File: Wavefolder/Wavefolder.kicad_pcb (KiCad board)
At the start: 2 copper layers, 25 x 200 mm, 39 parts, among them J1 Sig1, J2 EuroPower, J3 Sig2, J4 Out1, J5 Out2, J6 CV2, Q1 BC547, Q2 BC557, Q3 BC557, Q4 BC547, Q5 BC557, Q6 BC547, U1 TL074, U2 TL082, U3 TL074

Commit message: Wavefolder layout
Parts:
- removed D6: LED, LED_SMD:LED_1206_3216Metric_ReverseMount_Hole1.8x2.4mm
- removed R10: 1k, Resistor_SMD:R_1206_3216Metric_Pad1.42x1.75mm_HandSolder
- added D1: 1N4148, Diode_THT:D_DO-35_SOD27_P7.62mm_Horizontal, F.Cu at (21.1, 120.6)
- added D2: 1N4148, Diode_THT:D_DO-35_SOD27_P7.62mm_Horizontal, F.Cu at (35.7, 105.3)
- added D4: 1N4148, Diode_THT:D_DO-35_SOD27_P7.62mm_Horizontal, F.Cu at (33.2, 105.3)
- added R15: 100k, Resistor_SMD:R_1206_3216Metric_Pad1.42x1.75mm_HandSolder, B.Cu at (13.4, 180.3)
- added R16: 100k, Resistor_SMD:R_1206_3216Metric_Pad1.42x1.75mm_HandSolder, B.Cu at (14.1, 175.3)
- added R17: 100k, Resistor_THT:R_Axial_DIN0204_L3.6mm_D1.6mm_P7.62mm_Horizontal, F.Cu at (26.1, 115.6)
- added R18: 100k, Resistor_THT:R_Axial_DIN0204_L3.6mm_D1.6mm_P7.62mm_Horizontal, F.Cu at (24.0, 115.6)
- added R19: 100k, Resistor_THT:R_Axial_DIN0204_L3.6mm_D1.6mm_P7.62mm_Horizontal, F.Cu at (26.5, 102.8)
- added R20: 100k, Resistor_THT:R_Axial_DIN0204_L3.6mm_D1.6mm_P7.62mm_Horizontal, F.Cu at (28.4, 102.8)
- added R21: 100k, Resistor_THT:R_Axial_DIN0204_L3.6mm_D1.6mm_P2.54mm_Vertical, F.Cu at (16.8, 102.8)
- added R22: 100k, Resistor_THT:R_Axial_DIN0204_L3.6mm_D1.6mm_P7.62mm_Horizontal, B.Cu at (22.8, 110.4)
- added R23: 15k, Resistor_THT:R_Axial_DIN0204_L3.6mm_D1.6mm_P7.62mm_Horizontal, B.Cu at (22.8, 108.0)
- added R24: 15k, Resistor_THT:R_Axial_DIN0204_L3.6mm_D1.6mm_P7.62mm_Horizontal, B.Cu at (32.8, 110.3)
- added R25: 1k, Resistor_SMD:R_1206_3216Metric_Pad1.42x1.75mm_HandSolder, B.Cu at (14.2, 201.5)
- added R26: 100k, Resistor_SMD:R_1206_3216Metric_Pad1.42x1.75mm_HandSolder, B.Cu at (13.8, 163.7)
- added R27: 100k, Resistor_SMD:R_1206_3216Metric_Pad1.42x1.75mm_HandSolder, B.Cu at (28.8, 145.1)
- added R28: 100k, Resistor_SMD:R_1206_3216Metric_Pad1.42x1.75mm_HandSolder, B.Cu at (28.2, 140.1)
- added R29: 100k, Resistor_SMD:R_1206_3216Metric_Pad1.42x1.75mm_HandSolder, B.Cu at (28.9, 135.0)
- added U4: TL082, Package_SO:SOIC-8_3.9x4.9mm_P1.27mm, B.Cu at (14.9, 187.0)
- R1, R11, R12, R13, R14, R2, R5, R6, R8, R9: footprint Resistor_THT:R_Axial_DIN0204_L3.6mm_D1.6mm_P7.62mm_Horizontal -> Resistor_THT:R_Axial_DIN0204_L3.6mm_D1.6mm_P2.54mm_Vertical
- R3: moved to B.Cu
- R4, R7: footprint Resistor_THT:R_Axial_DIN0204_L3.6mm_D1.6mm_P7.62mm_Horizontal -> Resistor_THT:R_Axial_DIN0204_L3.6mm_D1.6mm_P2.54mm_Vertical; moved to B.Cu
- U2: footprint Package_DIP:DIP-8_W7.62mm_LongPads -> Package_SO:SOIC-8_3.9x4.9mm_P1.27mm; moved to B.Cu
- moved C1 60.8 mm to (2.40, 87.6)
- moved C2 60.8 mm to (7.80, 88.1)
- moved R1 39.0 mm to (19.7, 92.9), turned to 270 degrees
- moved R14 37.5 mm to (16.4, 79.6), turned to 0 degrees
- moved D3 33.9 mm to (13.7, 118.0)
- moved R11 33.7 mm to (27.8, 100.2)
- moved R2 32.1 mm to (19.7, 100.2)
- moved R4 28.1 mm to (29.6, 87.1), turned to 0 degrees
- moved R3 27.8 mm to (19.4, 87.2), turned to 0 degrees
- moved R5 26.4 mm to (35.9, 100.2)
- moved R13 25.1 mm to (21.0, 79.6), turned to 0 degrees
- moved R9 22.2 mm to (34.8, 79.6), turned to 270 degrees
- moved RV2 20.5 mm to (22.0, 145.1)
- moved R7 20.0 mm to (27.1, 85.0), turned to 0 degrees
- moved R8 19.7 mm to (32.1, 79.6), turned to 180 degrees
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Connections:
- D3 pad 1: Net-(D3-Pad1) -> Net-(D1-Pad1)
- D3 pad 2: Net-(D3-Pad2) -> /~Sig2
- R13 pad 1: Net-(Q5-Pad1) -> Net-(R13-Pad1)
- R13 pad 2: Net-(R13-Pad2) -> Net-(Q5-Pad1)
- R14 pad 1: Net-(R13-Pad2) -> /Out1
- R14 pad 2: /Out1 -> Net-(R13-Pad1)
- R8 pad 1: Net-(R7-Pad2) -> Net-(R8-Pad1)
- R8 pad 2: Net-(R8-Pad2) -> Net-(R7-Pad2)
- R9 pad 1: Net-(R8-Pad2) -> Net-(R8-Pad1)
- RV2 pad 2: Net-(RV2-Pad2) -> Net-(R26-Pad2)
- RV2 pad 3: Net-(RV2-Pad3) -> Net-(R26-Pad2)
- RV3 pad 1: Net-(RV3-Pad1) -> +12V
- RV3 pad 3: Net-(RV3-Pad3) -> -12V
- U1 pad 1: (no net) -> Net-(Q1-Pad2)
- U1 pad 13: Net-(R13-Pad2) -> Net-(R13-Pad1)
- U1 pad 2: (no net) -> Net-(Q1-Pad2)
- U1 pad 3: (no net) -> Net-(RV1-Pad2)
- U1 pad 8: Net-(R8-Pad2) -> Net-(R8-Pad1)
- U2 pad 1: Net-(U2-Pad1) -> /Offset
- U2 pad 3: Net-(U2-Pad3) -> Net-(RV3-Pad2)
- U2 pad 5: Net-(U2-Pad5) -> GND
- U2 pad 6: Net-(U2-Pad6) -> Net-(R26-Pad2)
- U3 pad 1: (no net) -> /~Offset
- U3 pad 10: (no net) -> /Offset
- U3 pad 11: (no net) -> -12V
- U3 pad 12: (no net) -> /~Offset
- U3 pad 13: (no net) -> Net-(R18-Pad2)
- U3 pad 14: (no net) -> /Bottom
- U3 pad 2: (no net) -> Net-(R19-Pad2)
- U3 pad 3: (no net) -> GND
- U3 pad 4: (no net) -> +12V
- U3 pad 5: Net-(U3-Pad5) -> Net-(D1-Pad1)
- U3 pad 6: Net-(U3-Pad6) -> Net-(D2-Pad1)
- U3 pad 7: Net-(U3-Pad7) -> Net-(D2-Pad1)
- U3 pad 8: (no net) -> /Top
- U3 pad 9: (no net) -> Net-(R17-Pad2)
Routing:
- net +12V: track 0.00 -> 247.2 mm, vias 0 -> 4
- net -12V: track 0.00 -> 229.7 mm, vias 0 -> 4
- net /Out2: track 0.00 -> 105.4 mm, vias 0 -> 1
- net /~Sig2: track 0.00 -> 98.9 mm, vias 0 -> 1
- net Net-(RV1-Pad2): track 0.00 -> 63.7 mm
- net /Offset: track 0.00 -> 40.6 mm, vias 0 -> 2
- net Net-(R26-Pad2): track 0.00 -> 38.6 mm
- net Net-(Q5-Pad2): track 0.00 -> 32.7 mm
- net /Sig2: track 0.00 -> 28.5 mm
- net Net-(D1-Pad1): track 0.00 -> 25.8 mm
- net /Bottom: track 0.00 -> 23.5 mm
- net Net-(Q5-Pad1): track 0.00 -> 20.3 mm
- net Net-(J5-PadT): track 0.00 -> 18.0 mm
- net Net-(Q3-Pad1): track 0.00 -> 17.5 mm
- net Net-(Q1-Pad1): track 0.00 -> 17.3 mm
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- added copper zone on B.Cu, net GND

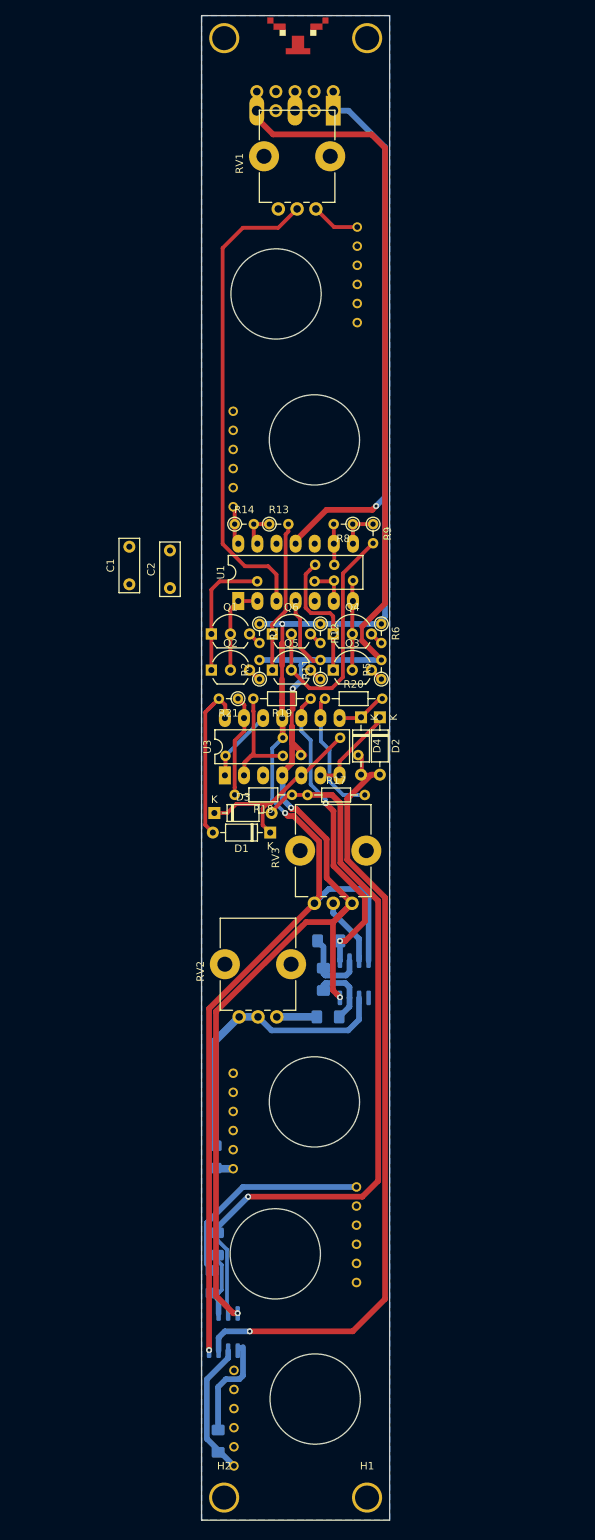
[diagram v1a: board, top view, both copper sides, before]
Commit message: Wavefolder design
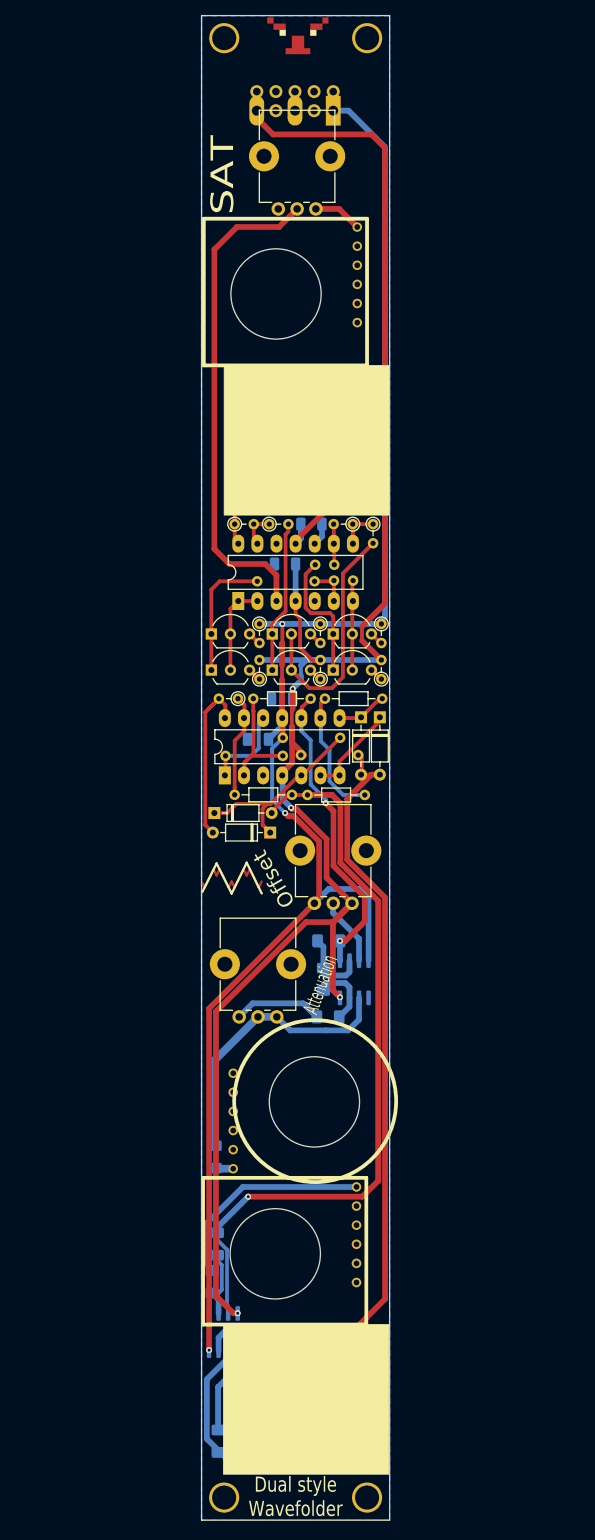
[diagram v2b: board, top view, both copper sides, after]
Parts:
- removed the R20 at (28.4, 102.8)
- removed the R21 at (16.8, 102.8)
- added C3: 100n, Capacitor_SMD:C_1206_3216Metric, B.Cu at (22.7, 102.8)
- added C4: 100n, Capacitor_SMD:C_1206_3216Metric, B.Cu at (19.5, 108.2)
- added R25: 100k, Resistor_THT:R_Axial_DIN0204_L3.6mm_D1.6mm_P7.62mm_Horizontal, F.Cu at (28.4, 102.8)
- added R27: 15k, Resistor_THT:R_Axial_DIN0204_L3.6mm_D1.6mm_P7.62mm_Horizontal, B.Cu at (32.8, 110.3)
- C1, C2: footprint Capacitor_THT:C_Disc_D7.0mm_W2.5mm_P5.00mm -> Capacitor_SMD:C_1206_3216Metric; moved to B.Cu
- R14: renamed from R26; value 100k -> 47k
- R15: renamed from R27; value 100k -> 4k7
- R16: renamed from R28; value 100k -> 47k
- R17: renamed from R29; value 100k -> 47k
- R18: renamed from R15; value 100k -> 47k
- R20: renamed from R16; value 100k -> 47k
- R24: value 15k -> 100k; footprint Resistor_THT:R_Axial_DIN0204_L3.6mm_D1.6mm_P7.62mm_Horizontal -> Resistor_THT:R_Axial_DIN0204_L3.6mm_D1.6mm_P2.54mm_Vertical; moved to F.Cu
- moved C1 20.9 mm to (23.1, 84.9), turned to 0 degrees
- moved C2 20.6 mm to (26.6, 79.6), turned to 180 degrees
- moved R24 17.7 mm to (16.8, 102.8)
- renumbered D3 to D2, D2 to D3, J2 to J1, J1 to J2, J4 to J3, J3 to J4, J6 to J5, J5 to J6, Q2 to Q1, Q1 to Q2, R2 to R1, R11 to R10, R12 to R11, R13 to R12, R14 to R13, R1 to R2, R22 to R21, R18 to R22, R17 to R23, R23 to R26, R25 to R28, RV3 to RV2, RV2 to RV3, U4 to U3, U3 to U4
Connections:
- R14 pad 2: Net-(R26-Pad2) -> Net-(R14-Pad2)
- R15 pad 1: Net-(R27-Pad1) -> Net-(R15-Pad1)
- R22 pad 2: Net-(R18-Pad2) (its old number) -> Net-(R22-Pad2)
- R24 pad 1: /Out2 -> Net-(R22-Pad2)
- R24 pad 2: +12V -> /Bottom
- RV3 pad 1: Net-(R27-Pad1) -> Net-(R14-Pad2)
- RV3 pad 2: Net-(R26-Pad2) -> Net-(R14-Pad2)
- RV3 pad 3: Net-(R26-Pad2) -> Net-(R15-Pad1)
- U2 pad 6: Net-(R26-Pad2) -> Net-(R14-Pad2)
- U4 pad 13: Net-(R18-Pad2) (its old number) -> Net-(R22-Pad2)
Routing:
- net Net-(R26-Pad2): track 38.6 -> 0.00 mm
- net Net-(R14-Pad2): track 0.00 -> 37.2 mm
- net Net-(R22-Pad2): track 0.00 -> 13.7 mm
- net Net-(R18-Pad2) (its old number): track 13.7 -> 0.00 mm
- net Net-(R15-Pad1): track 0.00 -> 11.8 mm
- net -12V: track 229.7 -> 236.1 mm
- net +12V: track 247.2 -> 253.4 mm
- net Net-(R27-Pad1): track 5.32 -> 0.00 mm
- net GND: track 2.54 -> 5.54 mm
- net Net-(RV1-Pad2): track 63.7 -> 66.2 mm
- net /~Offset: track 9.75 -> 11.7 mm
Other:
- board text added: "Attenuation"
- board text added: "CV"
- board text added: "Design by Adamski A. organfairy"
- board text added: "Dual style Wavefolder"
- board text added: "IN"
- board text added: "OUT"
- board text added: "Offset"
- board text added: "SAT"

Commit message: fixing folder case...
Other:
- board text added: "PCB ref here:"
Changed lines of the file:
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@@
   (general
     (thickness 1.6)
-    (drawings 54)
+    (drawings 59)
     (tracks 339)
     (zones 0)
@@
     )
   )
+  (gr_text "PCB ref here:" (at 24.5 12.9) (layer B.SilkS)
+    (effects (font (size 1 1) (thickness 0.15)) (justify mirror))
+  )
+  (gr_line (start 30.3 12) (end 18.9 12) (layer B.SilkS) (width 0.15))
+  (gr_line (start 18.9 12) (end 18.9 16.3) (layer B.SilkS) (width 0.15))
+  (gr_line (start 18.9 16.3) (end 30.3 16.3) (layer B.SilkS) (width 0.15))
+  (gr_line (start 30.3 16.3) (end 30.3 12) (layer B.SilkS) (width 0.15))
   (gr_line (start 12.1 127.3) (end 12.4 127.9) (layer F.Cu) (width 0.3))
   (gr_line (start 20 127.1) (end 19.6 127.9) (layer F.Cu) (width 0.3))

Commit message: Wavefolder done and tested!
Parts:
- added R13.1: 1k, Resistor_THT:R_Axial_DIN0204_L3.6mm_D1.6mm_P2.54mm_Vertical, F.Cu at (14.0, 82.1)
- moved R8 0.40 mm to (32.5, 79.6)
- moved R12 0.30 mm to (20.7, 79.6)
- moved R13 0.30 mm to (16.1, 79.6)
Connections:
- J3 pad T: /Out1 -> Net-(J3-PadT)
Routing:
- net Net-(J3-PadT): track 0.00 -> 3.18 mm
- net Net-(RV1-Pad2): track 66.2 -> 67.4 mm
- net /Out1: track 5.19 -> 5.84 mm
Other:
- board text added: "+12V"
- board text added: "-12V"
- board text added: "GND"

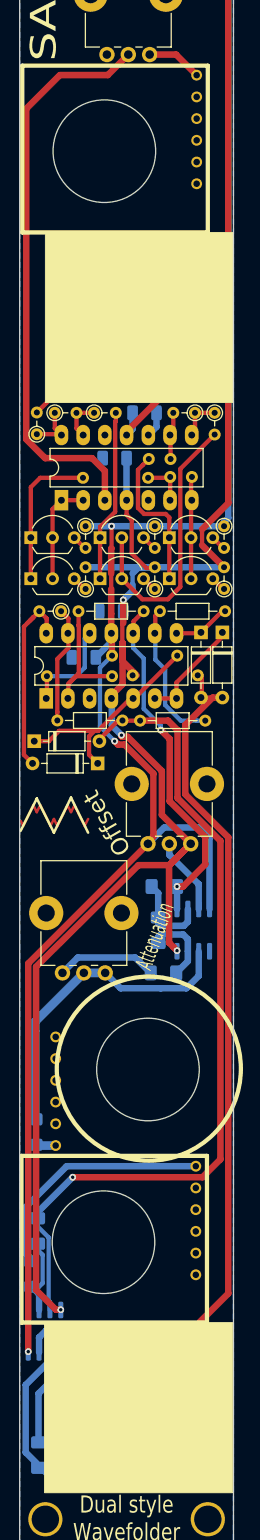
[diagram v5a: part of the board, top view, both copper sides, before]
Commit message: updated footprints on Wavefolder
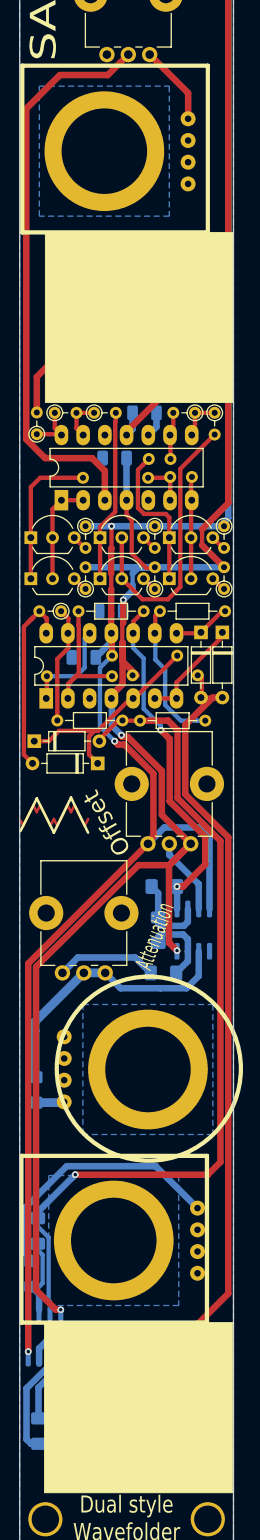
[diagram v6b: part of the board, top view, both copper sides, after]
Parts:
- J2, J3, J4, J5, J6: footprint telec:JackHole -> telec:Jack_Hole_Square
- moved R14 4.93 mm to (13.8, 158.8)
- moved R28 2.81 mm to (14.2, 198.7)
- moved J4 1.22 mm to (23.0, 176.4)
- moved U3 0.68 mm to (14.9, 187.7)
- moved J6 0.50 mm to (27.1, 196.4)
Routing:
- net Net-(R28-Pad1): track 14.3 -> 8.13 mm
- net Net-(J3-PadT): track 3.18 -> 8.70 mm
- net Net-(R14-Pad2): track 37.2 -> 32.2 mm
- net /Sig1: track 6.49 -> 9.37 mm
- net /Sig2: track 28.5 -> 30.7 mm
- net Net-(J6-PadT): track 18.0 -> 16.3 mm
- net /CV2: track 2.44 -> 3.44 mm
- net /Out2: track 105.4 -> 105.9 mm

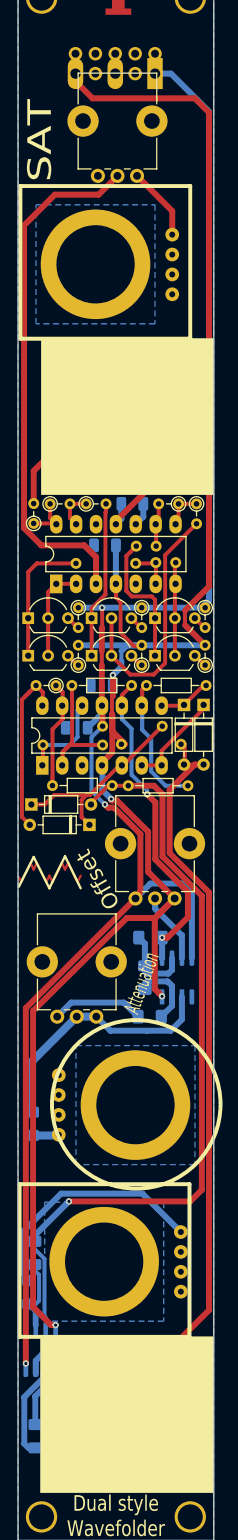
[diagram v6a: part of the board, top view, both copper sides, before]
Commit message: More clearance
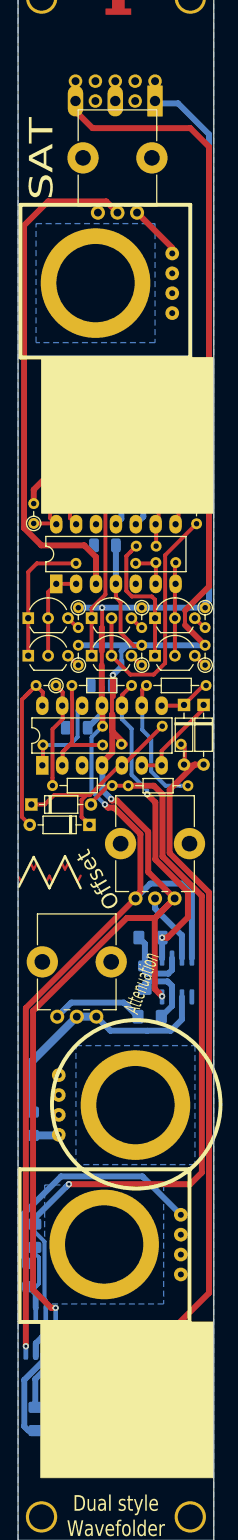
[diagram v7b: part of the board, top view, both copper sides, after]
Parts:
- moved RV1 4.70 mm to (27.2, 42.4)
- moved J1 3.50 mm to (29.5, 28.1)
- moved J2 2.40 mm to (21.9, 51.4)
- moved J3 2.40 mm to (27.0, 70.8)
- moved J4 2.20 mm to (23.0, 174.2)
- moved J6 2.20 mm to (27.1, 194.2)
- moved U3 2.20 mm to (14.9, 185.5)
- moved R18 2.20 mm to (13.4, 178.1)
- moved R20 2.20 mm to (14.1, 173.1)
- moved R28 2.20 mm to (14.2, 196.5)
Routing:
- net -12V: track 236.1 -> 228.9 mm, vias 4 -> 5
- net +12V: track 253.4 -> 247.1 mm
- net Net-(J3-PadT): track 8.70 -> 6.30 mm
- net /Sig1: track 9.37 -> 7.07 mm
- net /~Sig2: track 99.1 -> 96.9 mm
- net /Out2: track 105.9 -> 103.7 mm
- net Net-(RV1-Pad2): track 67.4 -> 66.6 mm
